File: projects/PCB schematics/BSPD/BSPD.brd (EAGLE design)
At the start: 160 x 100 mm, 83 parts, among them IC1 OP11D, IC10 4020D, IC11 74LS32D, IC12 74LS32D, IC2 OP11D, IC3 74LS32D, IC4 NE555D, IC5 4020D, IC6 OP11D, IC7 74LS32D, IC8 74ALS09D, IC9 74AHC1G04DBV, X1 5566-2, X2 5566-2, X3 5566-4

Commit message: BSPD - Initial placement.
Parts have been laid down in a preliminary placement. Routing for power will first be done, and then autorouting will be caried out for signals. Autorouting must be reviewed and redone manually.
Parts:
- removed IC1, IC2, IC6: OP11D, linear:SO14
- removed IC10, IC5: 4020D, 40xx:SO16
- removed IC11, IC12, IC3, IC7: 74LS32D, 74xx-us:SO14
- removed IC4: NE555D, linear:SO08
- removed IC8: 74ALS09D, 74xx-us:SO14
- removed IC9: 74AHC1G04DBV, 74xx-little-us:SOT23-5
- removed RN4: (no value), resistor-dil:SOMC16
- added AND1: 74ALS09D, 74xx-us:SO14
- added COUNT1, COUNT2: 4020D, 40xx:SO16
- added NE555D: NE555D, linear:SO08
- added NOT1: 74AHC1G04DBV, 74xx-little-us:SOT23-5
- added OP1, OP2, OP3: OP11D, linear:SO14
- added OR1, OR2, OR3, OR4: 74LS32D, 74xx-us:SO14
- added RN3: (no value), resistor-dil:SOMC16
- C1: device rcl:085CS_1AR -> rcl:C0805
- moved JP6 171.5 mm to (83.8, 21.6), turned to 270 degrees
- moved R28 161.3 mm to (74.9, 63.5), turned to 180 degrees
- moved JP5 160.9 mm to (91.4, 59.7), turned to 180 degrees
- moved R6 159.9 mm to (74.9, 52.1)
- moved JP10 158.5 mm to (94.0, 12.7), turned to 270 degrees
- moved R27 155.0 mm to (74.9, 59.7), turned to 180 degrees
- moved JP4 150.3 mm to (91.4, 64.8), turned to 180 degrees
- moved JP9 144.9 mm to (88.9, 12.7), turned to 270 degrees
- moved R25 144.5 mm to (74.9, 39.4)
- moved C7 140.1 mm to (57.1, 61.0)
- moved C6 137.7 mm to (57.1, 48.3)
- moved R24 137.6 mm to (74.9, 43.2)
- moved JP8 136.3 mm to (94.0, 21.6), turned to 270 degrees
- moved R7 136.2 mm to (47.2, 76.5), turned to 270 degrees
- moved JP3 131.3 mm to (82.5, 64.8), turned to 180 degrees
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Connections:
- net +0.5V: now also OP1.5, OP2.5; no longer IC1.5, IC2.5
- net +4.5V: now also OP1.2, OP2.2; no longer IC1.2, IC2.2
- net +5V: now also C1.1, NE555D.4, NE555D.8, RN3.1; no longer C1.+, IC4.4, IC4.8, RN4.1
- net BSE_PROCESSED: now also OP1.3, OP1.6, OP3.3; no longer IC2.3, IC2.6, IC6.3
- net BSPDFAULT: now also OR2.11; no longer IC7.11
- net BSPDPLAUS1: now also OR1.3; no longer IC3.3
- net BSPDPLAUS2: now also OR1.6; no longer IC3.6
- net GND: now also AND1.7, C1.2, NE555D.1, NOT1.3, OR1.7, OR2.7, OR3.7, OR4.7, RN3.9; no longer C1.-, IC11.7, IC12.7, IC3.7, IC4.1, IC7.7, IC8.7, IC9.3, RN4.9
- net MOTCUR_PROCESSED: now also OP2.3, OP2.6, OP3.5; no longer IC1.3, IC1.6, IC6.5
- net N$10: now also OP1.12; no longer IC2.12
- net N$100: now also COUNT1.1, JP5.1; no longer IC5.1, JP7.1
- net N$101: now also COUNT2.1; no longer IC10.1
- net N$102: now also OR3.13, OR3.8; no longer IC11.13, IC11.8
- net N$103: now also OR3.3, OR4.1; no longer IC11.3, IC12.1
- net N$104: now also OR3.6, OR4.2; no longer IC11.6, IC12.2
- net N$105: now also OR3.11, OR4.5; no longer IC11.11, IC12.5
- net N$11: now also OP2.1; no longer IC1.1
- net N$12: now also OP2.10; no longer IC1.10
- net N$13: now also OP2.12; no longer IC1.12
- net N$14: now also OP2.7; no longer IC1.7
- net N$15: now also OR2.3, OR2.5; no longer IC7.3, IC7.5
- net N$16: now also RN1.2; no longer RN4.2
- net N$17: now also AND1.3, AND1.5, COUNT2.11, NOT1.2; no longer IC10.11, IC8.3, IC8.5, IC9.2
- net N$18: now also OR1.8, OR2.9; no longer IC3.8, IC7.9
- net N$19: now also OP3.2, RN1.16; no longer IC6.2, RN4.16
- net N$20: now also OR1.9; no longer IC3.9
- net N$21: now also OP3.6, RN2.16; no longer IC6.6, RN1.16
- net N$22: now also AND1.10, AND1.4, NE555D.3; no longer IC4.3, IC8.10, IC8.4
- net N$23: now also OR2.12, OR2.8; no longer IC7.12, IC7.8
- net N$25: now also NE555D.5; no longer IC4.5
- net N$26: now also AND1.2, OP3.7; no longer IC6.7, IC8.2
- net N$27: now also AND1.1, OP3.1; no longer IC6.1, IC8.1
- net N$29: now also AND1.9, NOT1.4; no longer IC8.9, IC9.4
- net N$3: now also COUNT1.3, OR2.4; no longer IC5.3, IC7.4
- net N$31: now also JP6.2, OR3.1; no longer IC11.1, JP4.2
- net N$32: now also COUNT2.13, JP6.1; no longer IC10.13, JP4.1
- net N$33: now also JP7.2, OR3.2; no longer IC11.2, JP5.2
- net N$34: now also JP8.2, OR3.4; no longer IC11.4, JP6.2
- net N$35: now also COUNT2.14, JP8.1; no longer IC10.14, JP6.1
- net N$36: now also OR3.5; no longer IC11.5
- net N$37: now also OR3.9; no longer IC11.9
- net N$38: now also COUNT2.2, OR3.10; no longer IC10.2, IC11.10
- net N$39: now also COUNT2.12, JP7.1; no longer IC10.12, JP5.1
- net N$40: now also COUNT1.13; no longer IC5.13
- net N$41: now also OR1.10; no longer IC3.10
- net N$42: now also AND1.8, COUNT2.10; no longer IC10.10, IC8.8
- net N$43: now also AND1.6, COUNT1.10; no longer IC5.10, IC8.6
- net N$44: now also OP1.8, OR1.1; no longer IC2.8, IC3.1
- net N$45: now also OP1.14, OR1.2; no longer IC2.14, IC3.2
- net N$46: now also OP2.8, OR1.4; no longer IC1.8, IC3.4
- net N$47: now also OP2.14, OR1.5; no longer IC1.14, IC3.5
- net N$48: now also OR1.12; no longer IC3.12
- net N$49: now also COUNT1.14; no longer IC5.14
- net N$50: now also JP4.2, OR1.13; no longer IC3.13, JP8.2
- net N$51: now also JP5.2, OR2.1; no longer IC7.1, JP7.2
- net N$52: now also COUNT2.15; no longer IC10.15
- net N$53: now also OR4.3, OR4.4; no longer IC12.3, IC12.4
- net N$54: now also COUNT2.3, OR3.12; no longer IC10.3, IC11.12
- net N$55: now also COUNT1.2, OR2.2; no longer IC5.2, IC7.2
- net N$56: now also OR1.11, OR2.10; no longer IC3.11, IC7.10
- net N$57: now also RN1.3; no longer RN4.3
- net N$58: now also RN1.4; no longer RN4.4
- net N$59: now also RN1.5; no longer RN4.5
- net N$60: now also RN1.6; no longer RN4.6
- net N$61: now also NE555D.7; no longer IC4.7
- net N$62: now also RN1.7; no longer RN4.7
- net N$63: now also RN1.8; no longer RN4.8
- net N$64: now also RN1.15; no longer RN4.15
- net N$65: now also RN1.14; no longer RN4.14
- net N$66: now also RN1.13; no longer RN4.13
- net N$67: now also RN1.12; no longer RN4.12
- net N$68: now also RN1.11; no longer RN4.11
- net N$69: now also RN1.10; no longer RN4.10
- net N$7: now also OP1.1; no longer IC2.1
- net N$70: now also COUNT1.15, JP4.1; no longer IC5.15, JP8.1
- net N$71: now also RN2.2; no longer RN1.2
- net N$72: now also RN2.3; no longer RN1.3
- net N$73: now also RN2.4; no longer RN1.4
- net N$74: now also RN2.5; no longer RN1.5
- net N$75: now also RN2.6; no longer RN1.6
- net N$76: now also RN2.7; no longer RN1.7
- net N$77: now also RN2.8; no longer RN1.8
- net N$78: now also RN2.15; no longer RN1.15
- net N$79: now also RN2.14; no longer RN1.14
- net N$8: now also OP1.7; no longer IC2.7
- net N$80: now also RN2.13; no longer RN1.13
- net N$81: now also RN2.12; no longer RN1.12
- net N$82: now also RN2.11; no longer RN1.11
- net N$83: now also RN2.10; no longer RN1.10
- net N$84: now also RN3.2; no longer RN2.2
- net N$85: now also RN3.3; no longer RN2.3
- net N$86: now also RN3.4; no longer RN2.4
- net N$87: now also RN3.5; no longer RN2.5
- net N$88: now also RN3.6; no longer RN2.6
- net N$89: now also RN3.7; no longer RN2.7
- net N$9: now also OP1.10; no longer IC2.10
- net N$90: now also RN3.8; no longer RN2.8
- net N$91: now also RN3.15; no longer RN2.15
- net N$92: now also RN3.14; no longer RN2.14
- net N$93: now also RN3.13; no longer RN2.13
- net N$94: now also RN3.12; no longer RN2.12
- net N$95: now also RN3.11; no longer RN2.11
- net N$96: now also RN3.10; no longer RN2.10
- net N$97: now also COUNT1.12; no longer IC5.12
- net N$98: now also OR2.13, OR2.6; no longer IC7.13, IC7.6
- net RESET_FAULTCOUNT: now also COUNT1.11, OR4.6; no longer IC12.6, IC5.11
- net TIME_THRESH: now also OP1.13, OP1.9, OP2.13, OP2.9, RN3.16; no longer IC1.13, IC1.9, IC2.13, IC2.9, RN2.16
- net TR: now also NE555D.2, NE555D.6; no longer IC4.2, IC4.6
- net V+: now also OP1.4, OP2.4, OP3.4; no longer IC1.4, IC2.4, IC6.4
- net V-: now also OP1.11, OP2.11, OP3.11; no longer IC1.11, IC2.11, IC6.11
- net VCC: now also AND1.14, NOT1.5, OR1.14, OR2.14, OR3.14, OR4.14; no longer IC11.14, IC12.14, IC3.14, IC7.14, IC8.14, IC9.5
- net VDD: now also COUNT1.16, COUNT2.16; no longer IC10.16, IC5.16
- net VSS: now also COUNT1.8, COUNT2.8; no longer IC10.8, IC5.8
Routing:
- net +5V: track 0.00 -> 7.33 mm
- net N$4: track 0.00 -> 3.93 mm
- net N$1: track 0.00 -> 3.81 mm
- net +4.0V: track 0.00 -> 2.86 mm
- net +1.0V: track 0.00 -> 2.86 mm
- net N$5: track 0.00 -> 2.78 mm
- net +4.5V: track 0.00 -> 2.78 mm
- net N$2: track 0.00 -> 2.77 mm
- net N$6: track 0.00 -> 2.73 mm
- net +0.5V: track 0.00 -> 2.54 mm
- added copper zone on layer 1, net GND
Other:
- board size 160 x 100 mm -> 99.1 x 99.1 mm
- board text added: "1. BSE_PROCESSED 2. MOTCUR_PROCESSED"
- board text added: "1. BSPDPLAUS1 2. BSPDPLAUS2 3. BSPDFAULT"
- board text added: "Author: github.com/michaelpass"
- board text added: "Brake System Plausibility Device (BSPD) Board Rev A: 04/01/19"
- board text added: "INPUT"
- board text added: "Inputs:"
- board text added: "Iowa Formula"
- board text added: "OUTPUT"
- board text added: "Outputs:"
- board text added: "POWER"

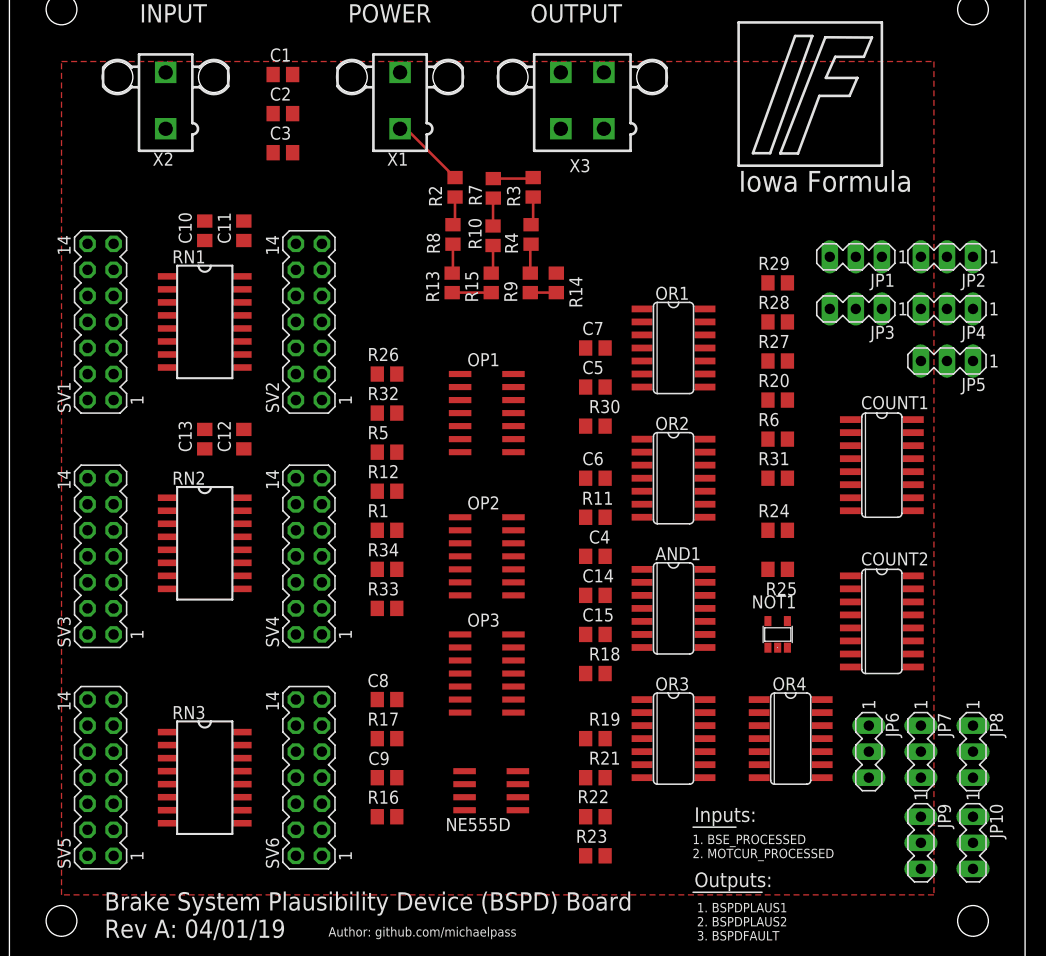
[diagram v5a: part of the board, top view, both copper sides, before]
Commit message: BSPD - Hand routing complete.
Proceding with auto routing.

Squashed - BSPD - Initial routing.

Routing underway. Ground pour chosen. Routing easy choices before attempting autorouting.
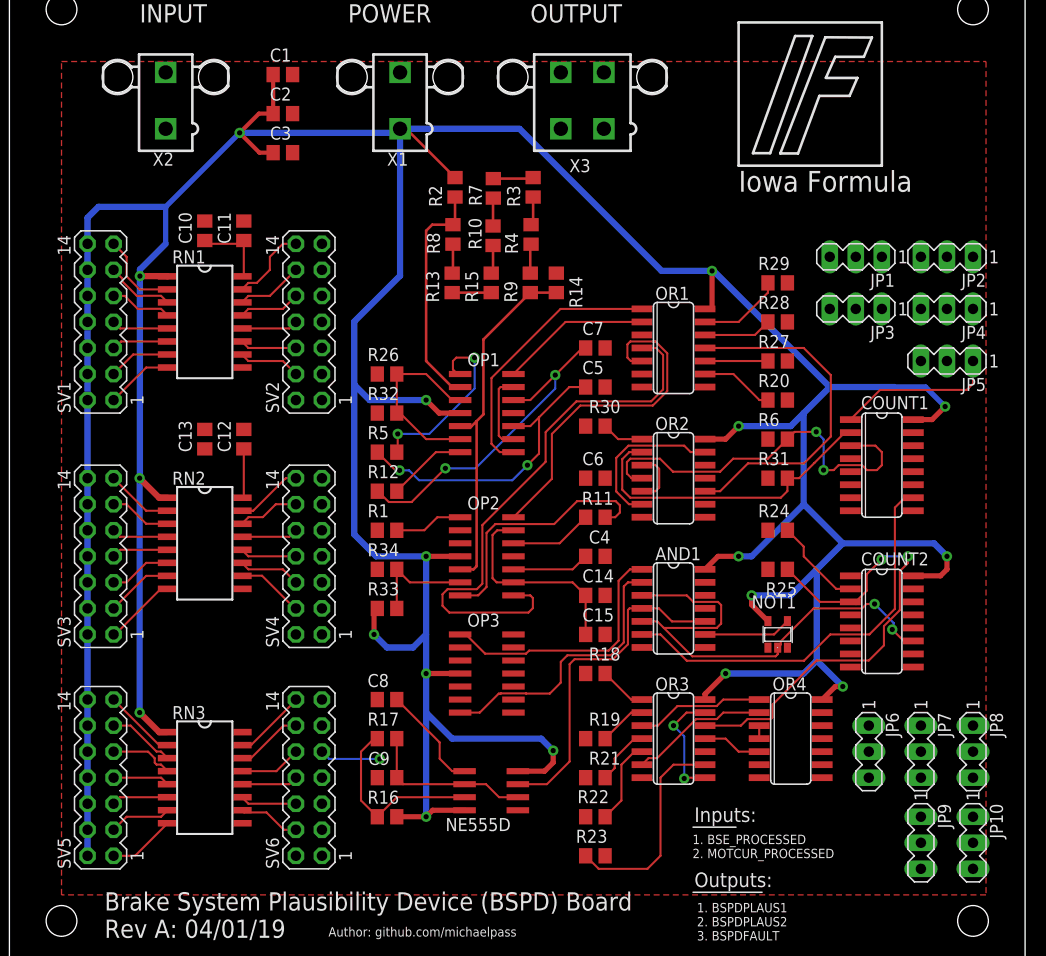
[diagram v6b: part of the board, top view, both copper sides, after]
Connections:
- removed net V+: OP1.4, OP2.4, OP3.4
- removed net V-: OP1.11, OP2.11, OP3.11
- removed net VCC: AND1.14, NOT1.5, OR1.14, OR2.14, OR3.14, OR4.14
- removed net VDD: COUNT1.16, COUNT2.16
- removed net VSS: COUNT1.8, COUNT2.8
- net +5V: now also AND1.14, COUNT1.16, COUNT2.16, NOT1.5, OP1.4, OP2.4, OP3.4, OR1.14, OR2.14, OR3.14, OR4.14
- net GND: now also COUNT1.8, COUNT2.8, OP1.11, OP2.11, OP3.11
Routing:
- net +5V: track 7.33 -> 471.8 mm, vias 0 -> 18
- net N$46: track 0.00 -> 53.9 mm
- net N$17: track 0.00 -> 48.5 mm, vias 0 -> 2
- net N$54: track 0.00 -> 46.6 mm, vias 0 -> 2
- net N$43: track 0.00 -> 39.9 mm
- net N$3: track 0.00 -> 38.4 mm, vias 0 -> 2
- net N$56: track 0.00 -> 33.8 mm
- net N$47: track 0.00 -> 33.7 mm
- net N$22: track 0.00 -> 33.4 mm
- net N$10: track 0.00 -> 32.8 mm, vias 0 -> 2
- net +0.5V: track 2.54 -> 35.0 mm
- net N$55: track 0.00 -> 31.1 mm
- net N$9: track 0.00 -> 30.1 mm, vias 0 -> 2
- net TIME_THRESH: track 0.00 -> 27.7 mm
- net N$26: track 0.00 -> 27.4 mm
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
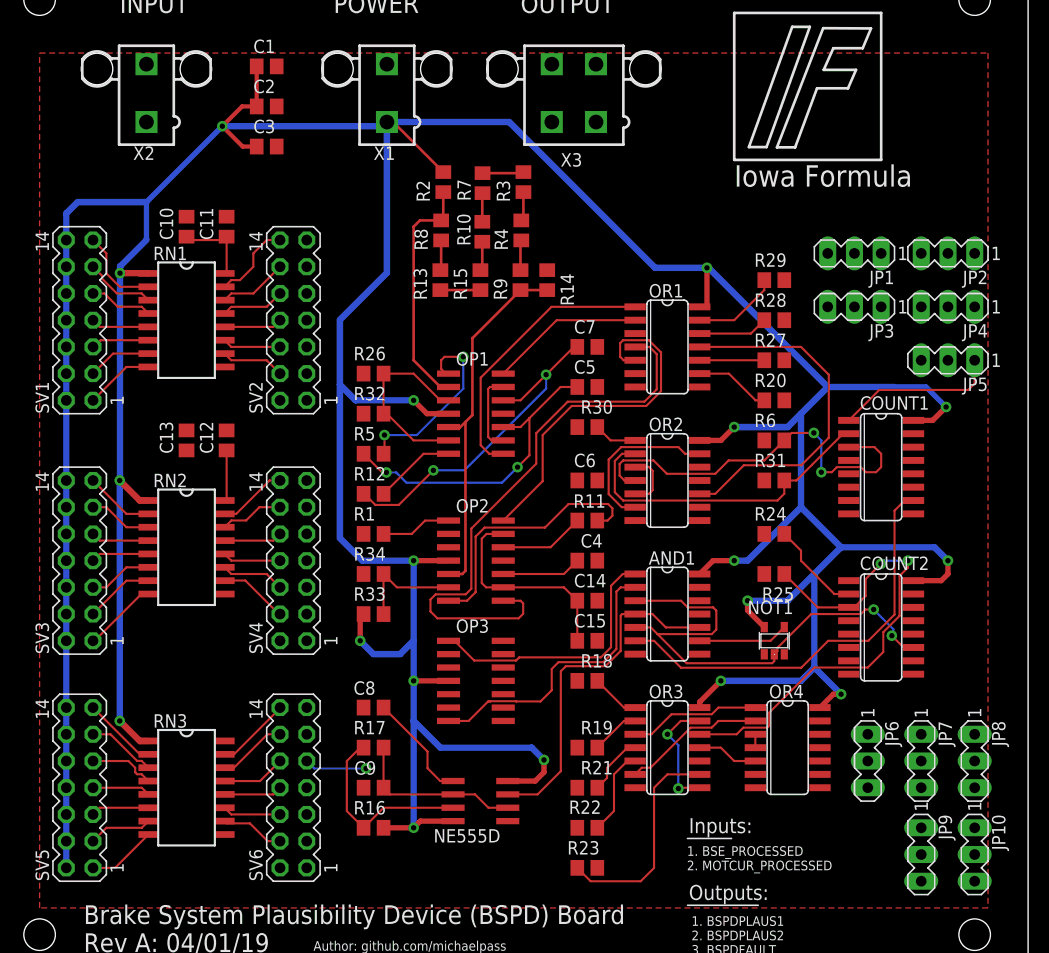
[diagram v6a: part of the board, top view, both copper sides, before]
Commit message: BSPD - Auto-routing complete.
Performed autorouting. Results generally good. Must correct for ground islands left.

Must touch up board clearances. BSPD otherwise done.
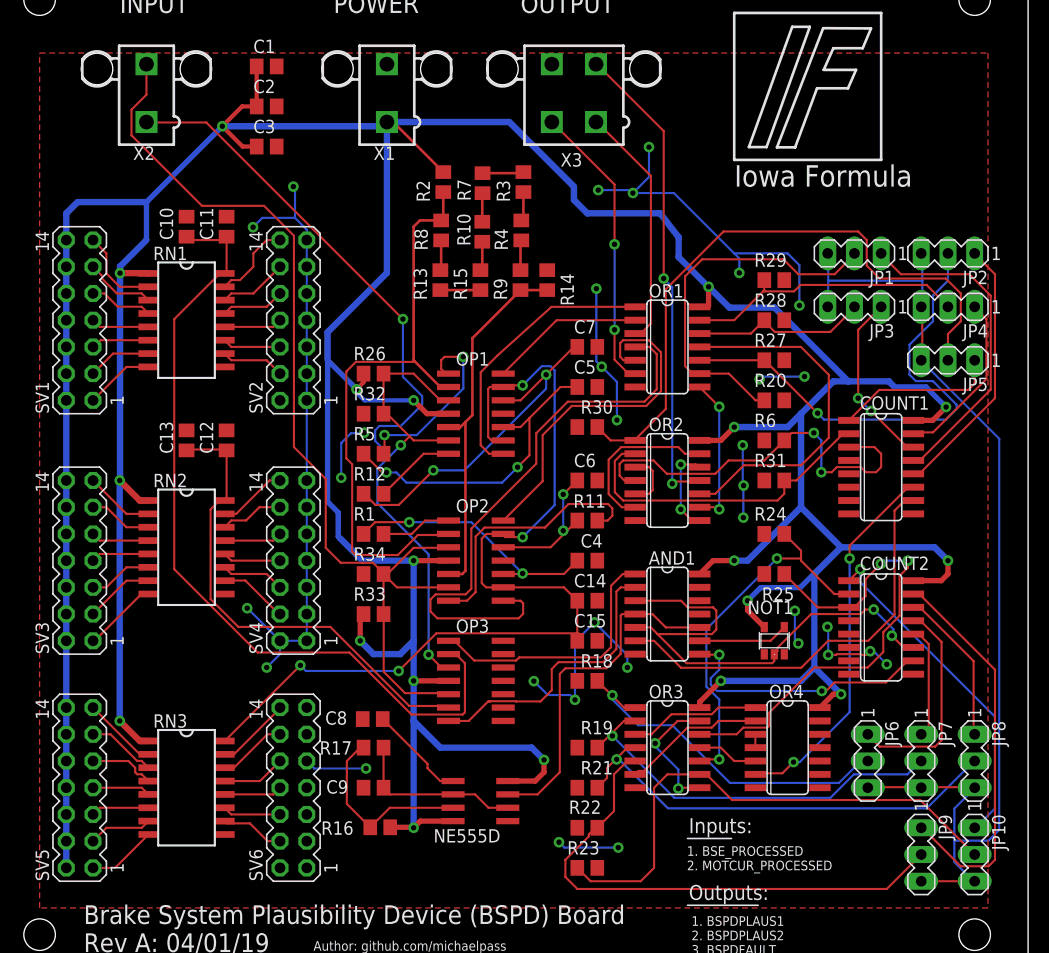
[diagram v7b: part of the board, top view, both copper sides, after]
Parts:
- moved C8 1.09 mm to (36.8, 25.6)
- moved R16 0.64 mm to (37.5, 15.3)
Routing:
- net GND: track 5.93 -> 164.2 mm, vias 1 -> 32
- net N$99: track 0.00 -> 102.6 mm
- net MOTCUR_PROCESSED: track 10.5 -> 94.7 mm
- net BSE_PROCESSED: track 18.3 -> 94.3 mm, vias 0 -> 3
- net N$19: track 7.52 -> 77.9 mm
- net TIME_THRESH: track 27.7 -> 91.8 mm, vias 0 -> 4
- net N$51: track 4.12 -> 60.7 mm
- net BSPDFAULT: track 0.00 -> 45.6 mm, vias 0 -> 2
- net N$36: track 7.53 -> 50.0 mm
- net N$21: track 4.84 -> 45.9 mm
- net N$41: track 6.14 -> 46.3 mm, vias 0 -> 1
- net N$34: track 4.99 -> 43.7 mm, vias 0 -> 1
- net N$52: track 0.00 -> 37.6 mm
- net RESET_FAULTCOUNT: track 0.00 -> 35.6 mm, vias 0 -> 2
- net +4.5V: track 21.9 -> 57.1 mm
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
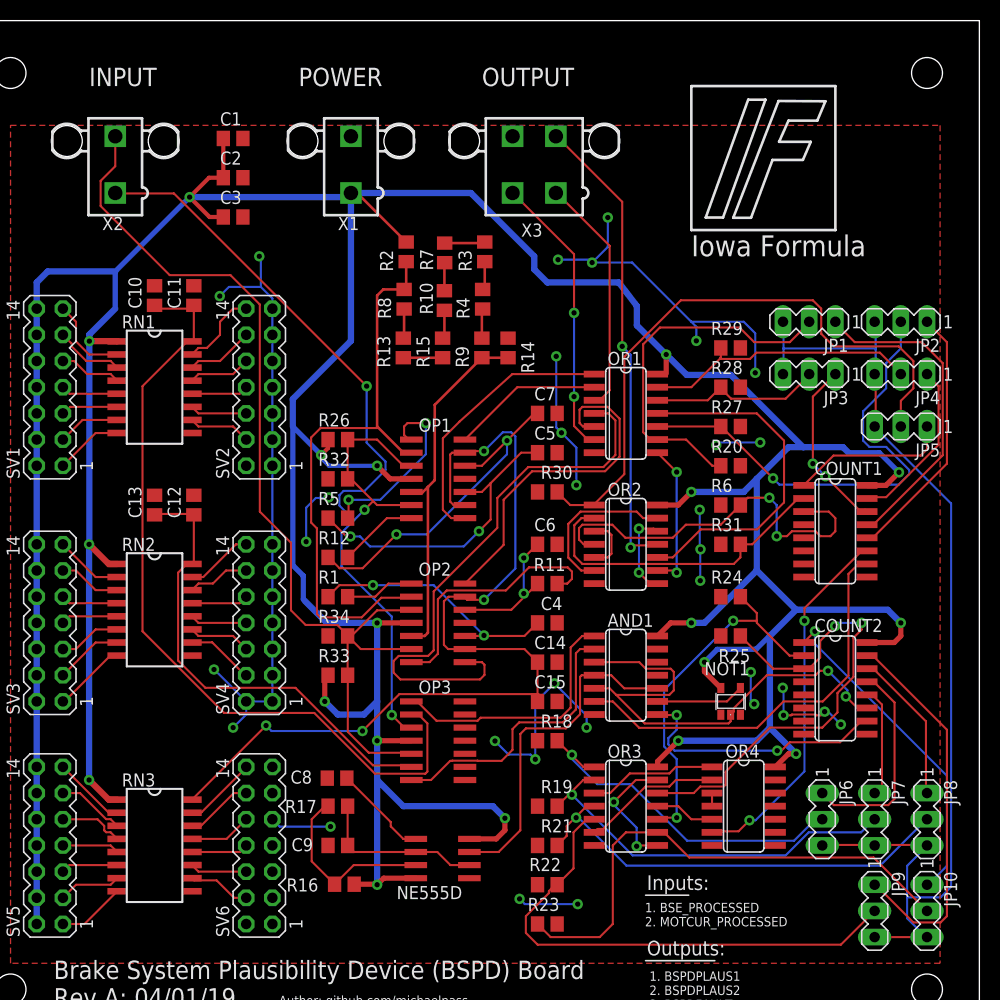
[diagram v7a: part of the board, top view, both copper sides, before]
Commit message: BSPD - Rev A; Gerber files.
Initial board revisions complete. This board represents a working draft. GERBER files have been generated. Please review.
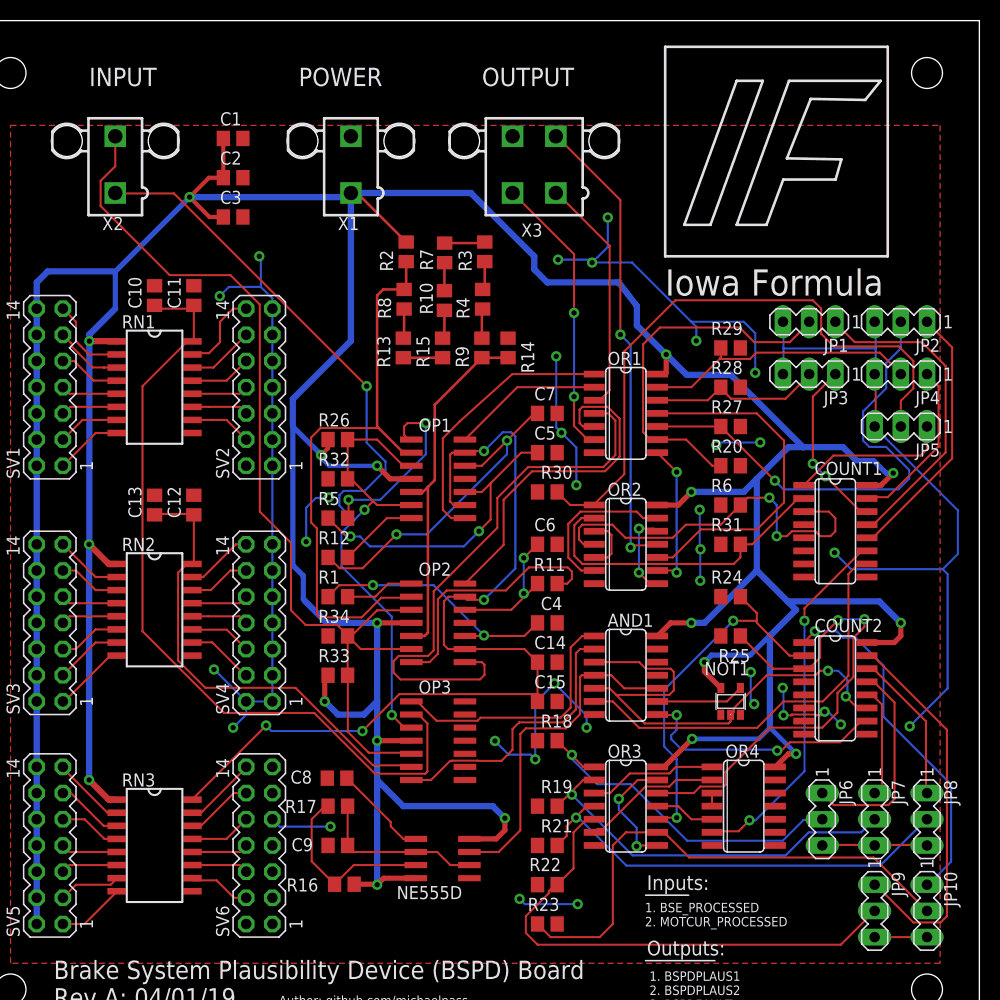
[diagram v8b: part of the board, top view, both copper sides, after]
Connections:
- removed net N$99: JP1.3, JP10.3, JP2.3, JP3.3, JP4.3, JP5.3, JP6.3, JP7.3, JP8.3, JP9.3
- net GND: now also JP1.3, JP10.3, JP2.3, JP3.3, JP4.3, JP5.3, JP6.3, JP7.3, JP8.3, JP9.3
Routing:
- net N$99: track 102.6 -> 0.00 mm
- net GND: track 164.2 -> 249.8 mm, vias 32 -> 34
- net N$101: track 32.3 -> 34.6 mm
- net N$54: track 46.9 -> 48.0 mm
- net N$42: track 25.8 -> 25.1 mm
- net N$41: track 46.3 -> 46.9 mm
- net N$17: track 48.5 -> 49.0 mm
- net N$102: track 12.4 -> 11.9 mm
